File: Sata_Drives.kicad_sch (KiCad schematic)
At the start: 1 part, among them IC3 ASM1352R

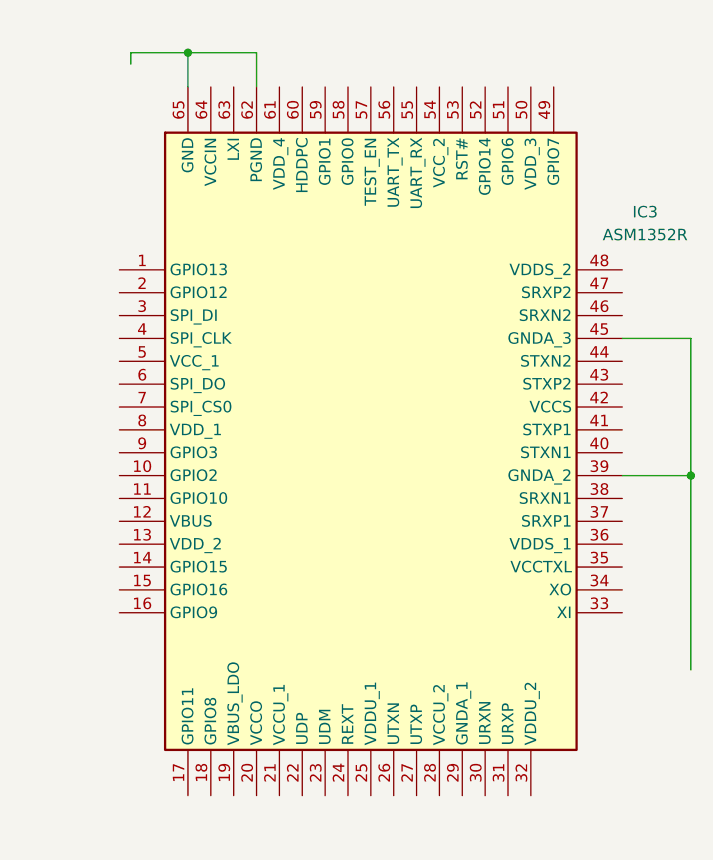
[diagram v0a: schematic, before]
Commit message: Notation changed on M.2 Sheet
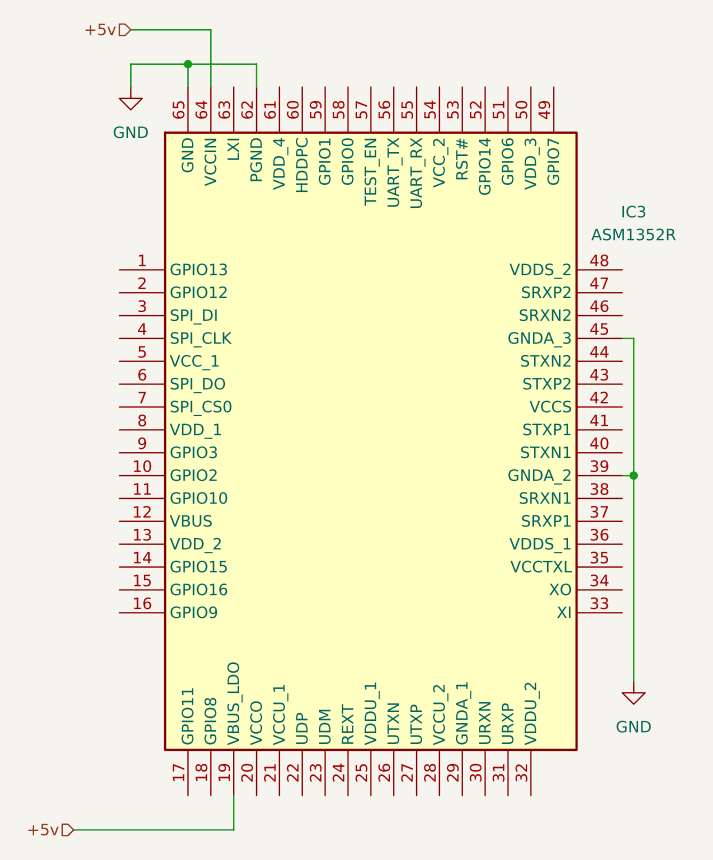
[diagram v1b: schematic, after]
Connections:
- net +5v: now reaches IC3.19 (VBUS_LDO)
- net +5v: now also IC3.64 (VCCIN)
- net GND: now reaches IC3.39 (GNDA_2), IC3.45 (GNDA_3)
- net GND: now also IC3.62 (PGND), IC3.65 (GND)
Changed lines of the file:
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@@
 	(paper "A4")
 	(junction
-		(at 157.48 78.74)
+		(at 151.13 78.74)
 		(diameter 0)
 		(color 0 0 0 0)
 	)
 	(junction
-		(at 101.6 31.75)
+		(at 101.6 33.02)
 		(diameter 0)
 		(color 0 0 0 0)
@@
 	(wire
 		(pts
-			(xy 101.6 35.56) (xy 101.6 31.75)
-		)
-		(stroke
-			(width 0)
-			(type default)
-		)
-	)
-	(wire
-		(pts
-			(xy 149.86 78.74) (xy 157.48 78.74)
-		)
-		(stroke
-			(width 0)
-			(type default)
-		)
-	)
-	(wire
-		(pts
-			(xy 95.25 31.75) (xy 95.25 33.02)
-		)
-		(stroke
-			(width 0)
-			(type default)
-		)
-	)
-	(wire
-		(pts
-			(xy 149.86 63.5) (xy 157.48 63.5)
-		)
-		(stroke
-			(width 0)
-			(type default)
-		)
-	)
-	(wire
-		(pts
-			(xy 101.6 31.75) (xy 109.22 31.75)
-		)
-		(stroke
-			(width 0)
-			(type default)
-		)
-	)
-	(wire
-		(pts
-			(xy 101.6 31.75) (xy 95.25 31.75)
-		)
-		(stroke
-			(width 0)
-			(type default)
-		)
-	)
-	(wire
-		(pts
-			(xy 109.22 35.56) (xy 109.22 31.75)
-		)
-		(stroke
-			(width 0)
-			(type default)
-		)
-	)
-	(wire
-		(pts
-			(xy 157.48 78.74) (xy 157.48 100.33)
-		)
-		(stroke
-			(width 0)
-			(type default)
-		)
-	)
-	(wire
-		(pts
-			(xy 157.48 63.5) (xy 157.48 78.74)
-		)
-		(stroke
-			(width 0)
-			(type default)
+			(xy 104.14 29.21) (xy 104.14 35.56)
+		)
+		(stroke
+			(width 0)
+			(type default)
+		)
+	)
+	(wire
+		(pts
+			(xy 101.6 35.56) (xy 101.6 33.02)
+		)
+		(stroke
+			(width 0)
+			(type default)
+		)
+	)
+	(wire
+		(pts
+			(xy 95.25 29.21) (xy 104.14 29.21)
+		)
+		(stroke
+			(width 0)
+			(type default)
+		)
+	)
+	(wire
+		(pts
+			(xy 106.68 114.3) (xy 106.68 118.11)
+		)
+		(stroke
+			(width 0)
+			(type default)
+		)
+	)
+	(wire
+		(pts
+			(xy 149.86 78.74) (xy 151.13 78.74)
+		)
+		(stroke
+			(width 0)
+			(type default)
+		)
+	)
+	(wire
+		(pts
+			(xy 95.25 33.02) (xy 95.25 35.56)
+		)
+		(stroke
+			(width 0)
+			(type default)
+		)
+	)
+	(wire
+		(pts
+			(xy 149.86 63.5) (xy 151.13 63.5)
+		)
+		(stroke
+			(width 0)
+			(type default)
+		)
+	)
+	(wire
+		(pts
+			(xy 106.68 118.11) (xy 88.9 118.11)
+		)
+		(stroke
+			(width 0)
+			(type default)
+		)
+	)
+	(wire
+		(pts
+			(xy 101.6 33.02) (xy 109.22 33.02)
+		)
+		(stroke
+			(width 0)
+			(type default)
+		)
+	)
+	(wire
+		(pts
+			(xy 101.6 33.02) (xy 95.25 33.02)
+		)
+		(stroke
+			(width 0)
+			(type default)
+		)
+	)
+	(wire
+		(pts
+			(xy 109.22 35.56) (xy 109.22 33.02)
+		)
+		(stroke
+			(width 0)
+			(type default)
+		)
+	)
+	(wire
+		(pts
+			(xy 151.13 78.74) (xy 151.13 101.6)
+		)
+		(stroke
+			(width 0)
+			(type default)
+		)
+	)
+	(wire
+		(pts
+			(xy 151.13 63.5) (xy 151.13 78.74)
+		)
+		(stroke
+			(width 0)
+			(type default)
+		)
+	)
+	(hierarchical_label "+5v"
+		(shape input)
+		(at 95.25 29.21 180)
+		(effects
+			(font
+				(size 1.27 1.27)
+			)
+			(justify right)
+		)
+	)
+	(hierarchical_label "+5v"
+		(shape input)
+		(at 88.9 118.11 180)
+		(effects
+			(font
+				(size 1.27 1.27)
+			)
+			(justify right)
+		)
+	)
+	(symbol
+		(lib_id "power:GND")
+		(at 95.25 35.56 0)
+		(unit 1)
+		(exclude_from_sim no)
+		(in_bom yes)
+		(on_board yes)
+		(dnp no)
+		(fields_autoplaced yes)
+		(property "Reference" "#PWR072"
+			(at 95.25 41.91 0)
+			(effects
+				(font
+					(size 1.27 1.27)
+				)
+				(hide yes)
+			)
+		)
+		(property "Value" "GND"
+			(at 95.25 40.64 0)
+			(effects
+				(font
+					(size 1.27 1.27)
+				)
+			)
+		)
+		(property "Footprint" ""
+			(at 95.25 35.56 0)
+			(effects
+				(font
+					(size 1.27 1.27)
+				)
+				(hide yes)
+			)
+		)
+		(property "Datasheet" ""
+			(at 95.25 35.56 0)
+			(effects
+				(font
+					(size 1.27 1.27)
+				)
+				(hide yes)
+			)
+		)
+		(property "Description" "Power symbol creates a global label with name \"GND\" , ground"
+			(at 95.25 35.56 0)
+			(effects
+				(font
+					(size 1.27 1.27)
+				)
+				(hide yes)
+			)
+		)
+		(pin "1"
+		)
+		(instances
+			(project ""
+				(path "/0650c7a8-acba-429c-9f8e-eec0baf0bc1c/fede4c36-00cc-4d3d-b71c-5243ba232202/a72edad3-d792-4f36-af8a-632fcfbc9d26"
+					(reference "#PWR072")
+					(unit 1)
+				)
+			)
 		)
 	)
@@
 		(fields_autoplaced yes)
 		(property "Reference" "IC3"
-			(at 152.4 49.4598 0)
+			(at 151.13 49.4598 0)
 			(effects
 				(font
@@
 		)
 		(property "Value" "ASM1352R"
-			(at 152.4 51.9998 0)
+			(at 151.13 51.9998 0)
 			(effects
 				(font
@@
 					(unit 1)
 				)
+			)
+		)
+	)
+	(symbol
+		(lib_id "power:GND")
+		(at 151.13 101.6 0)
+		(unit 1)
+		(exclude_from_sim no)
+		(in_bom yes)
+		(on_board yes)
+		(dnp no)
+		(fields_autoplaced yes)
+		(property "Reference" "#PWR079"
+			(at 151.13 107.95 0)
+			(effects
+				(font
+					(size 1.27 1.27)
+				)
+				(hide yes)
+			)
+		)
+		(property "Value" "GND"
+			(at 151.13 106.68 0)
+			(effects
+				(font
+					(size 1.27 1.27)
+				)
+			)
+		)
+		(property "Footprint" ""
+			(at 151.13 101.6 0)
+			(effects
+				(font
+					(size 1.27 1.27)
+				)
+				(hide yes)
+			)
+		)
+		(property "Datasheet" ""
+			(at 151.13 101.6 0)
+			(effects
+				(font
+					(size 1.27 1.27)
+				)
+				(hide yes)
+			)
+		)
+		(property "Description" "Power symbol creates a global label with name \"GND\" , ground"
+			(at 151.13 101.6 0)
+			(effects
+				(font
+					(size 1.27 1.27)
+				)
+				(hide yes)
+			)
+		)
+		(pin "1"
+		)
+		(instances
+			(project ""
+				(path "/0650c7a8-acba-429c-9f8e-eec0baf0bc1c/fede4c36-00cc-4d3d-b71c-5243ba232202/a72edad3-d792-4f36-af8a-632fcfbc9d26"
+					(reference "#PWR079")
+					(unit 1)
+				)
